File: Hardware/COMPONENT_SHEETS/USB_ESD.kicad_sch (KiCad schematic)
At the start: 9 parts, among them J4 10118192-0001LF, U4 LM317T, U5 USBLC6-2SC6

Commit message: Update item tags
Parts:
- D1: LCSC C189957 -> C239808
- U5: LCSC (none) -> C7519
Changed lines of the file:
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@@
       (effects (font (size 1.27 1.27)) hide)
     )
-    (property "LCSC" "C189957" (id 4) (at 119.38 82.55 0)
+    (property "LCSC" " C239808 " (id 4) (at 119.38 82.55 0)
       (effects (font (size 1.27 1.27)) hide)
     )
@@
       (effects (font (size 1.27 1.27)) hide)
     )
+    (property "LCSC" "C7519" (id 4) (at 219.71 96.52 0)
+      (effects (font (size 1.27 1.27)) hide)
+    )

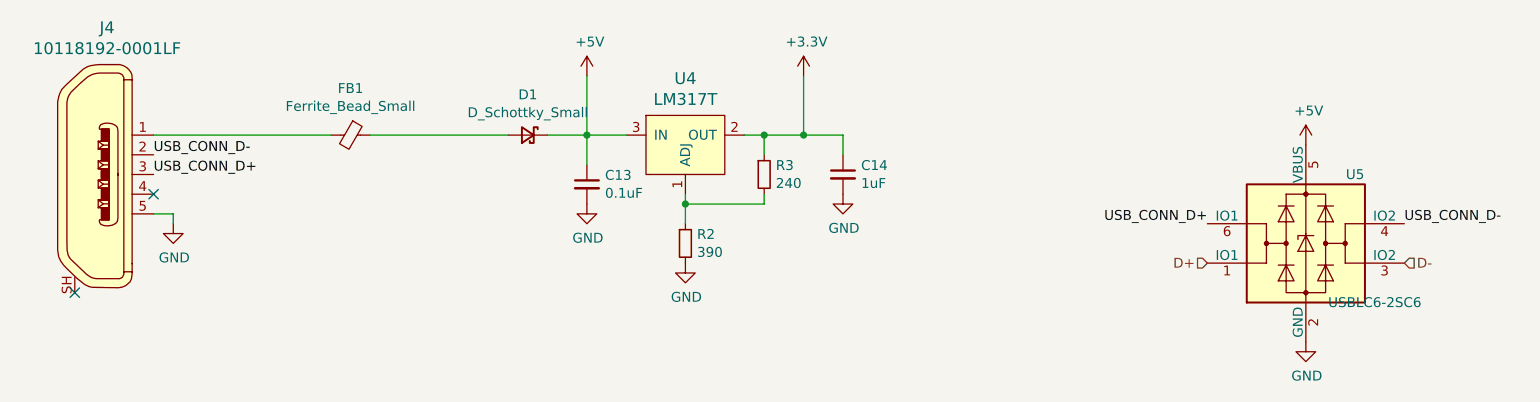
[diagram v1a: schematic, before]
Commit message: Adapted layout to different linear regulator for USB
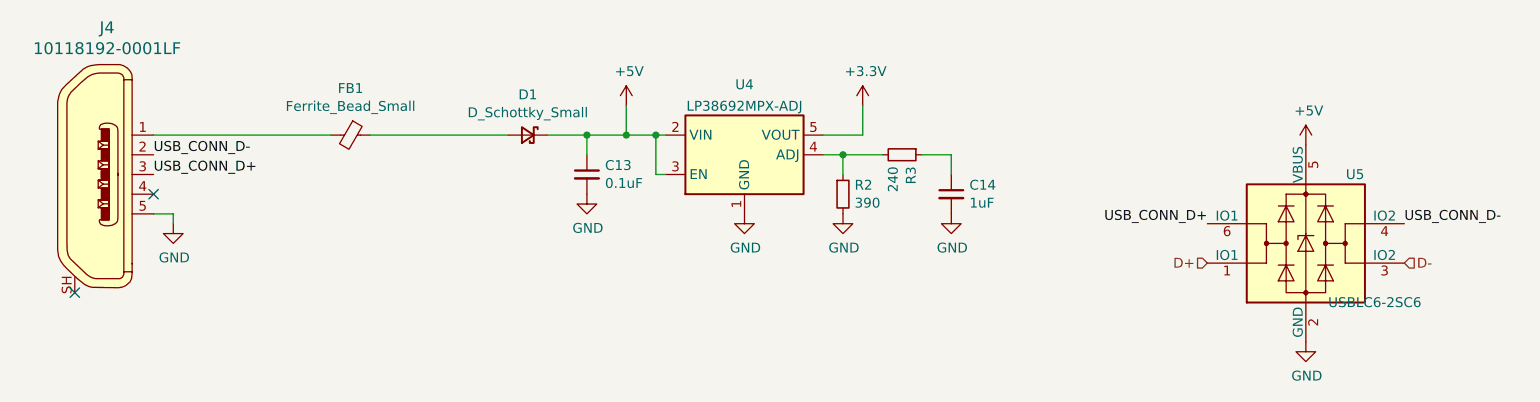
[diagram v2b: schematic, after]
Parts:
- removed U4: LM317T, Package_TO_SOT_SMD:TSOT-23, symbol dk_PMIC-Voltage-Regulators-Linear:LM317T
- added U4: LP38692MPX-ADJ, Package_TO_SOT_SMD:SOT-223-5, symbol Regulator_Linear:ADP7182AUJZ
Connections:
- net +3V3: now also U4.5 (VOUT); no longer C14.1, R3.1
- net +5V: now also U4.2 (VIN), U4.3 (EN)
- net GND: now also U4.1 (GND)
- net at R2.1, R3.2: now also U4.4 (ADJ)
- new net: C14.1, R3.1
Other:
- moved on the sheet: C13, C14, R2, R3

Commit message: Updated SMPS wiring and voltage regulator footprint
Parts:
- R2, R3: footprint Resistor_SMD:R_0603_1608Metric_Pad1.05x0.95mm_HandSolder -> Resistor_SMD:R_0603_1608Metric_Pad0.98x0.95mm_HandSolder
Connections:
- net +3V3: now also U4.3 (VOUT); no longer U4.5 (VOUT)
- net +5V: now also U4.1 (EN), U4.4 (VIN); no longer U4.2 (VIN), U4.3 (EN)
- net GND: now also U4.5 (GND); no longer U4.1 (GND)
- net at R2.1, R3.2: now also U4.2 (ADJ); no longer U4.4 (ADJ)
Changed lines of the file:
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@@
       (effects (font (size 1.27 1.27)) (justify left))
     )
-    (property "Footprint" "Resistor_SMD:R_0603_1608Metric_Pad1.05x0.95mm_HandSolder" (id 2) (at 160.02 90.17 0)
+    (property "Footprint" "Resistor_SMD:R_0603_1608Metric_Pad0.98x0.95mm_HandSolder" (id 2) (at 160.02 90.17 0)
       (effects (font (size 1.27 1.27)) hide)
     )
@@
       (effects (font (size 1.27 1.27)) (justify left))
     )
-    (property "Footprint" "Resistor_SMD:R_0603_1608Metric_Pad1.05x0.95mm_HandSolder" (id 2) (at 167.64 85.09 0)
+    (property "Footprint" "Resistor_SMD:R_0603_1608Metric_Pad0.98x0.95mm_HandSolder" (id 2) (at 167.64 85.09 0)
       (effects (font (size 1.27 1.27)) hide)
     )

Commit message: Adjusted 5V lines, corrected ground fences, added cutout for USB connector
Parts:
- D1: footprint Diode_SMD:D_0603_1608Metric_Pad1.05x0.95mm_HandSolder -> Diode_SMD:D_0805_2012Metric_Pad1.15x1.40mm_HandSolder
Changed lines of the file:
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@@
     (property "Reference" "D1" (id 0) (at 119.38 77.343 0))
     (property "Value" "D_Schottky_Small" (id 1) (at 119.38 79.6544 0))
-    (property "Footprint" "Diode_SMD:D_0603_1608Metric_Pad1.05x0.95mm_HandSolder" (id 2) (at 119.38 82.55 90)
+    (property "Footprint" "Diode_SMD:D_0805_2012Metric_Pad1.15x1.40mm_HandSolder" (id 2) (at 119.38 82.55 90)
       (effects (font (size 1.27 1.27)) hide)
     )

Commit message: Updated schematic labels, Version 2.0.0
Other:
- company: (none) -> When HAMs Fly Senior Design Team
- title: (none) -> USB and ESD Connections
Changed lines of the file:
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@@
 (kicad_sch (version 20211123) (generator eeschema)
   (paper "A4")
+  (title_block
+    (title "USB and ESD Connections")
+    (date "2022-03-24")
+    (rev "v2.0.0")
+    (company "When HAMs Fly Senior Design Team")
+    (comment 1 "https://github.com/MSTRocketDesignTeam/Avionics-Telemetry-PCB")
+    (comment 2 "Board Revision 2")
+    (comment 3 "Schematic depicting logical connections between components")
+  )
   (junction (at 132.08 82.55) (diameter 0) (color 0 0 0 0)
   )

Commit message: Changed D1 LCSC to make component fit on pads
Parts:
- D1: LCSC C239808 -> C22624
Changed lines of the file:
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@@
       (effects (font (size 1.27 1.27)) hide)
     )
-    (property "LCSC" " C239808 " (id 4) (at 119.38 82.55 0)
+    (property "LCSC" "C22624" (id 4) (at 119.38 82.55 0)
       (effects (font (size 1.27 1.27)) hide)
     )

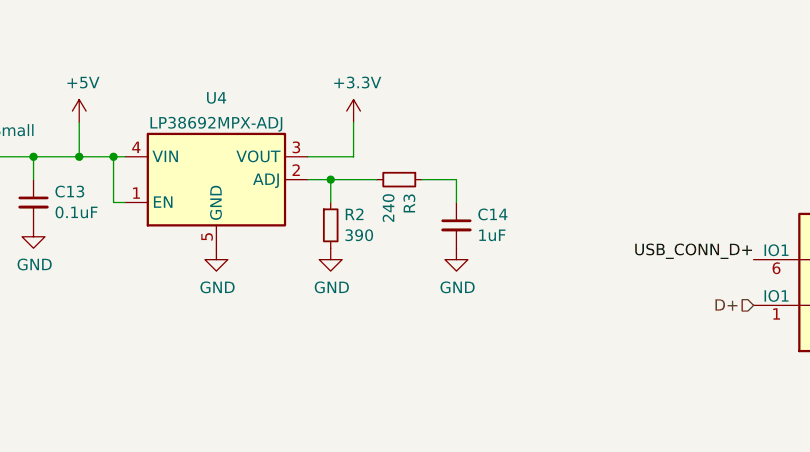
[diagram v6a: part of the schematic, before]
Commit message: Added more JLC part numbers and added missing voltage regulator connection
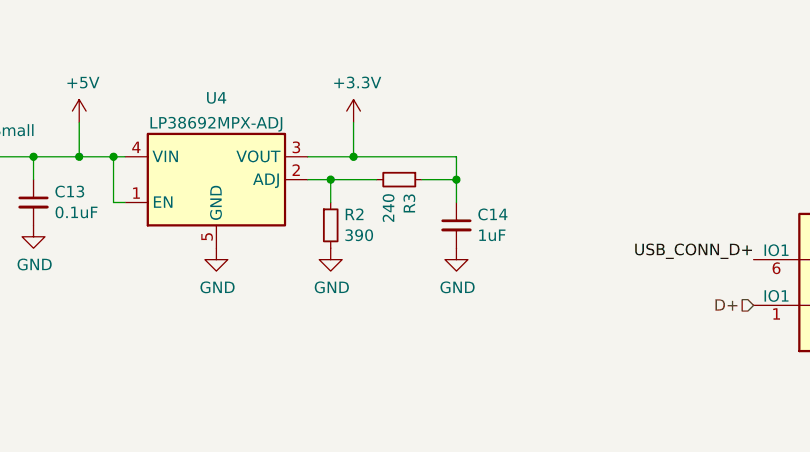
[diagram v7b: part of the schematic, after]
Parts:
- J4: LCSC (none) -> C132564
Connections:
- net +3V3: now also C14.1, R3.1
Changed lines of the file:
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@@
     (comment 3 "Schematic depicting logical connections between components")
+  )
+  (junction (at 173.99 85.09) (diameter 0) (color 0 0 0 0)
+  )
+  (junction (at 162.56 82.55) (diameter 0) (color 0 0 0 0)
   )
   (junction (at 132.08 82.55) (diameter 0) (color 0 0 0 0)
@@
     (stroke (width 0) (type default) (color 0 0 0 0))
   )
+  (wire (pts (xy 173.99 82.55) (xy 173.99 85.09))
+    (stroke (width 0) (type default) (color 0 0 0 0))
+  )
   (wire (pts (xy 173.99 85.09) (xy 170.18 85.09))
+    (stroke (width 0) (type default) (color 0 0 0 0))
+  )
+  (wire (pts (xy 162.56 82.55) (xy 173.99 82.55))
     (stroke (width 0) (type default) (color 0 0 0 0))
   )
@@
       (effects (font (size 1.524 1.524)) (justify left) hide)
     )
+    (property "LCSC" "C132564" (id 13) (at 63.5 87.63 0)
+      (effects (font (size 1.27 1.27)) hide)
+    )
     (pin "1")
